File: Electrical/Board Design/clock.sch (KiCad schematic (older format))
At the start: 46 parts, among them CON1 AVR-ISP-6, CON2 USB-MICRO-B, IC1 ATTINY84A-SS, P1 CONN_6, P2 CONN_2, P3 CONN_2, Q1 FET_N, Q2 FET_P, SW1 SPST, U1 MCP1624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

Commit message: board updates
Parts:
- R1: value 100K -> 0K
- R10, R11: value 50K -> 130K
- R3: value 100K -> 10K
- R7, R8: value 36K -> 33K
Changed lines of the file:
@@
 Sheet 1 1
 Title ""
-Date "17 apr 2015"
+Date "26 apr 2015"
 Rev ""
 Comp ""
@@
 P 6550 6900
 F 0 "R7" V 6630 6900 40  0000 C CNN
-F 1 "36K" V 6557 6901 40  0000 C CNN
+F 1 "33K" V 6557 6901 40  0000 C CNN
 F 2 "~" V 6480 6900 30  0000 C CNN
 F 3 "~" H 6550 6900 30  0000 C CNN
@@
 P 6550 7750
 F 0 "R8" V 6630 7750 40  0000 C CNN
-F 1 "36K" V 6557 7751 40  0000 C CNN
+F 1 "33K" V 6557 7751 40  0000 C CNN
 F 2 "~" V 6480 7750 30  0000 C CNN
 F 3 "~" H 6550 7750 30  0000 C CNN
@@
 P 12700 3950
 F 0 "R1" V 12780 3950 40  0000 C CNN
-F 1 "100K" V 12707 3951 40  0000 C CNN
+F 1 "0K" V 12707 3951 40  0000 C CNN
 F 2 "~" V 12630 3950 30  0000 C CNN
 F 3 "~" H 12700 3950 30  0000 C CNN
@@
 P 12700 5550
 F 0 "R3" V 12780 5550 40  0000 C CNN
-F 1 "100K" V 12707 5551 40  0000 C CNN
+F 1 "10K" V 12707 5551 40  0000 C CNN
 F 2 "~" V 12630 5550 30  0000 C CNN
 F 3 "~" H 12700 5550 30  0000 C CNN
@@
 P 8400 3850
 F 0 "R11" V 8480 3850 40  0000 C CNN
-F 1 "50K" V 8407 3851 40  0000 C CNN
+F 1 "130K" V 8407 3851 40  0000 C CNN
 F 2 "~" V 8330 3850 30  0000 C CNN
 F 3 "~" H 8400 3850 30  0000 C CNN
@@
 P 10600 3850
 F 0 "R10" V 10680 3850 40  0000 C CNN
-F 1 "50K" V 10607 3851 40  0000 C CNN
+F 1 "130K" V 10607 3851 40  0000 C CNN
 F 2 "~" V 10530 3850 30  0000 C CNN
 F 3 "~" H 10600 3850 30  0000 C CNN

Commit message: release board design
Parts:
- added P4: CONN_2, symbol CONN_2
- R10, R11: value 130K -> 51K
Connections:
- net GND: now also P4.2 (PM)
- net at C7.1, CON2.1 (VBUS), U2.2 (IN): now also P4.1 (P1)
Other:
- note added: "ALTERNATE FOR USB"
- moved on the sheet: C7, CON2, U2
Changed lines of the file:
@@
 Sheet 1 1
 Title ""
-Date "26 apr 2015"
+Date "6 jun 2015"
 Rev ""
 Comp ""
@@
 P 8400 3850
 F 0 "R11" V 8480 3850 40  0000 C CNN
-F 1 "130K" V 8407 3851 40  0000 C CNN
+F 1 "51K" V 8407 3851 40  0000 C CNN
 F 2 "~" V 8330 3850 30  0000 C CNN
 F 3 "~" H 8400 3850 30  0000 C CNN
@@
 P 10600 3850
 F 0 "R10" V 10680 3850 40  0000 C CNN
-F 1 "130K" V 10607 3851 40  0000 C CNN
+F 1 "51K" V 10607 3851 40  0000 C CNN
 F 2 "~" V 10530 3850 30  0000 C CNN
 F 3 "~" H 10600 3850 30  0000 C CNN
@@
 L USB-MICRO-B CON2
 U 1 1 54A87A25
-P 1850 1450
-F 0 "CON2" H 1550 1800 50  0000 C CNN
-F 1 "USB-MICRO-B" H 1700 1100 50  0000 C CNN
-F 2 "" H 1850 1350 50  0000 C CNN
-F 3 "" H 1850 1350 50  0000 C CNN
-	1    1850 1450
+P 2550 1450
+F 0 "CON2" H 2250 1800 50  0000 C CNN
+F 1 "USB-MICRO-B" H 2400 1100 50  0000 C CNN
+F 2 "" H 2550 1350 50  0000 C CNN
+F 3 "" H 2550 1350 50  0000 C CNN
+	1    2550 1450
 	1    0    0    -1
 $EndComp
@@
 L MCP1702T-1502E/TO U2
 U 1 1 54A87F96
-P 3200 1300
-F 0 "U2" H 3000 1500 40  0000 C CNN
-F 1 "MCP1702T-1502E/TO" H 3200 1500 40  0000 L CNN
-F 2 "TO-92" H 3200 1400 30  0000 C CIN
-F 3 "~" H 3200 1300 60  0000 C CNN
-	1    3200 1300
-	1    0    0    -1
-$EndComp
-Wire Wire Line
-	2650 1250 2800 1250
-Wire Wire Line
-	3200 2050 3200 1550
-Wire Wire Line
-	3600 1250 3950 1250
-Wire Wire Line
-	3950 1250 3950 2500
-Wire Wire Line
-	3950 2500 1800 2500
+P 4050 1300
+F 0 "U2" H 3850 1500 40  0000 C CNN
+F 1 "MCP1702T-1502E/TO" H 4050 1500 40  0000 L CNN
+F 2 "TO-92" H 4050 1400 30  0000 C CIN
+F 3 "~" H 4050 1300 60  0000 C CNN
+	1    4050 1300
+	1    0    0    -1
+$EndComp
+Wire Wire Line
+	3350 1250 3650 1250
+Wire Wire Line
+	4050 2100 4050 1550
+Wire Wire Line
+	4450 1250 4700 1250
+Wire Wire Line
+	4700 1250 4700 2500
+Wire Wire Line
+	4700 2500 1800 2500
 Connection ~ 1800 3600
 Wire Wire Line
-	2650 800  2650 1400
-Wire Wire Line
-	1100 800  2650 800
-Wire Wire Line
-	1100 1250 1100 800
-Connection ~ 1100 2050
+	3350 800  3350 1400
+Wire Wire Line
+	1800 800  3350 800
+Wire Wire Line
+	1800 800  1800 1250
 $Comp
 L GND #PWR026
 U 1 1 54A88164
-P 1100 2300
-F 0 "#PWR026" H 1100 2300 30  0001 C CNN
-F 1 "GND" H 1100 2230 30  0001 C CNN
-F 2 "" H 1100 2300 60  0000 C CNN
-F 3 "" H 1100 2300 60  0000 C CNN
-	1    1100 2300
-	1    0    0    -1
-$EndComp
-Wire Wire Line
-	1100 2050 3200 2050
-Wire Wire Line
-	1100 1650 1100 2300
-Wire Wire Line
-	1350 1650 1100 1650
-Wire Wire Line
-	1350 1250 1100 1250
+P 1800 2200
+F 0 "#PWR026" H 1800 2200 30  0001 C CNN
+F 1 "GND" H 1800 2130 30  0001 C CNN
+F 2 "" H 1800 2200 60  0000 C CNN
+F 3 "" H 1800 2200 60  0000 C CNN
+	1    1800 2200
+	1    0    0    -1
+$EndComp
+Wire Wire Line
+	1800 2100 4050 2100
+Wire Wire Line
+	1800 1650 1800 2200
+Wire Wire Line
+	2050 1650 1800 1650
+Wire Wire Line
+	1800 1250 2050 1250
 $Comp
 L C C7
 U 1 1 54A89CEC
-P 2650 1600
-F 0 "C7" H 2650 1700 40  0000 L CNN
-F 1 "1uF" H 2656 1515 40  0000 L CNN
-F 2 "~" H 2688 1450 30  0000 C CNN
-F 3 "~" H 2650 1600 60  0000 C CNN
-	1    2650 1600
-	1    0    0    -1
-$EndComp
-Connection ~ 2650 1250
-Wire Wire Line
-	2650 1800 2650 2050
-Connection ~ 2650 2050
+P 3350 1600
+F 0 "C7" H 3350 1700 40  0000 L CNN
+F 1 "1uF" H 3356 1515 40  0000 L CNN
+F 2 "~" H 3388 1450 30  0000 C CNN
+F 3 "~" H 3350 1600 60  0000 C CNN
+	1    3350 1600
+	1    0    0    -1
+$EndComp
+Connection ~ 3350 1250
+Wire Wire Line
+	3350 1800 3350 2100
 Text Label 7550 4200 0    60   ~ 0
 INT 1
@@
 	1    0    0    -1
 $EndComp
+$Comp
+L CONN_2 P4
+U 1 1 55690DE7
+P 1250 1400
+F 0 "P4" V 1200 1400 40  0000 C CNN
+F 1 "CONN_2" V 1300 1400 40  0000 C CNN
+F 2 "" H 1250 1400 60  0000 C CNN
+F 3 "" H 1250 1400 60  0000 C CNN
+	1    1250 1400
+	0    -1   -1   0
+$EndComp
+Wire Wire Line
+	1350 1750 1350 1900
+Wire Wire Line
+	1350 1900 1800 1900
+Connection ~ 1800 1900
+Wire Wire Line
+	1150 1750 1150 1900
+Wire Wire Line
+	1150 1900 700  1900
+Wire Wire Line
+	700  1900 700  900
+Wire Wire Line
+	700  900  1800 900
+Connection ~ 1800 900
+Text Notes 750  1250 0    60   ~ 0
+ALTERNATE FOR USB
+Connection ~ 3350 2100
+Connection ~ 1800 2100
 $EndSCHEMATC

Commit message: saved some circuit board updates
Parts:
- added P? (x2): CONN_2, symbol CONN_2
- added Q? (x3): FET_N, ~, symbol FET_N
- added Q?: FET_P, ~, symbol FET_P
- added R? (x3): 0K, ~, symbol R
- added R? (x2): 100K, ~, symbol POT
- added R? (x2): 10K, ~, symbol R
- added R? (x2): 100K, ~, symbol R
- added SW? (x2): SPST, ~, symbol SPST
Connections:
- net ALARM LIGHT: now also P?.1 (P1)
- net AM PM LIGHT: now also P?.1 (P1)
- net GND: now also P?.2 (PM), P?.2 (PM), Q?.S, Q?.S, R?.2, R?.2, SW?.2, SW?.2
- net MODE SELECT: now also R?.2, R?.2
- net MODE SELECT POWER: now also Q?.D, Q?.S, R?.1, R?.1, R?.1, R?.1
- net VCC: now also R?.2
- net at C7.1, CON2.1 (VBUS), P4.1 (P1)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: now also R?.1
- new net: Q?.D, R?.1, R?.2
- new net: Q?.D, R?.1, R?.3
- new net: Q?.G, Q?.G, R?.2, SW?.1
- new net: Q?.S, R?.1, R?.2
- new net: Q?.D, Q?.G, R?.1, R?.3
- new net: Q?.G, R?.2, SW?.1
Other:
- note added: "connectorized clock version\nand soldered flying lead version"
- note added: "jumper to optionally\ncircumvent power blocks\nfor alarm clock version"
- moved on the sheet: D1, D2, D3, R13, R14, R15, SP1

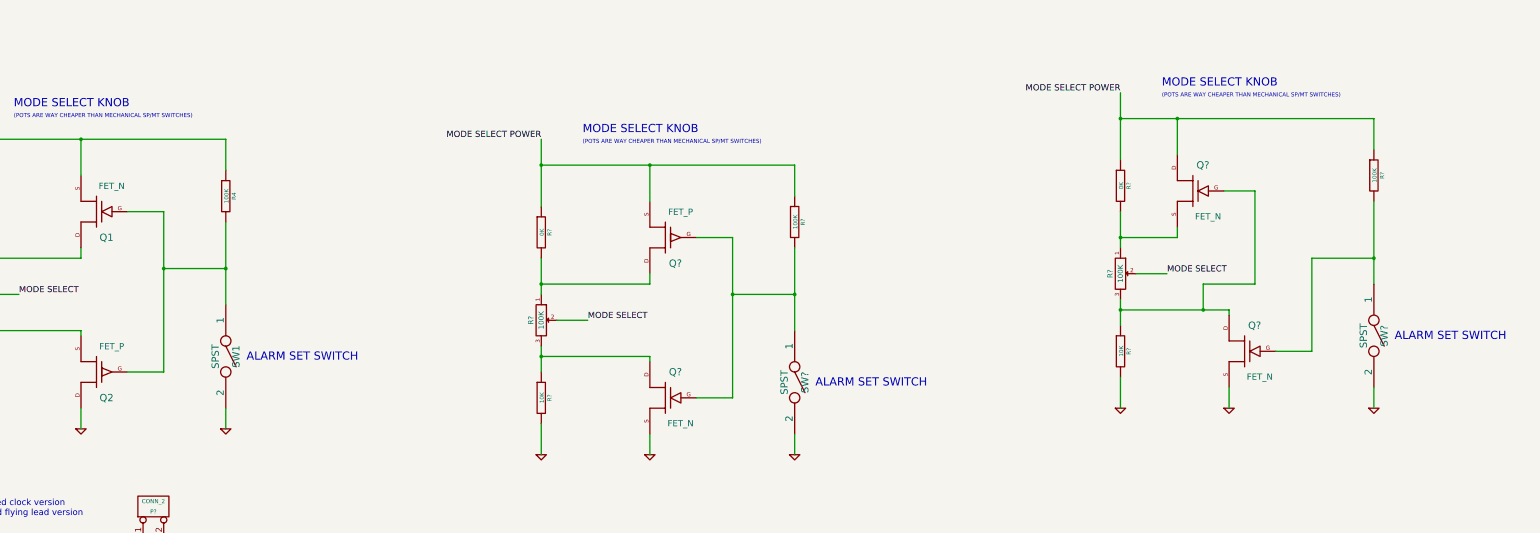
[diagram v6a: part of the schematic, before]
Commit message: fixed schematic
closes issue #17
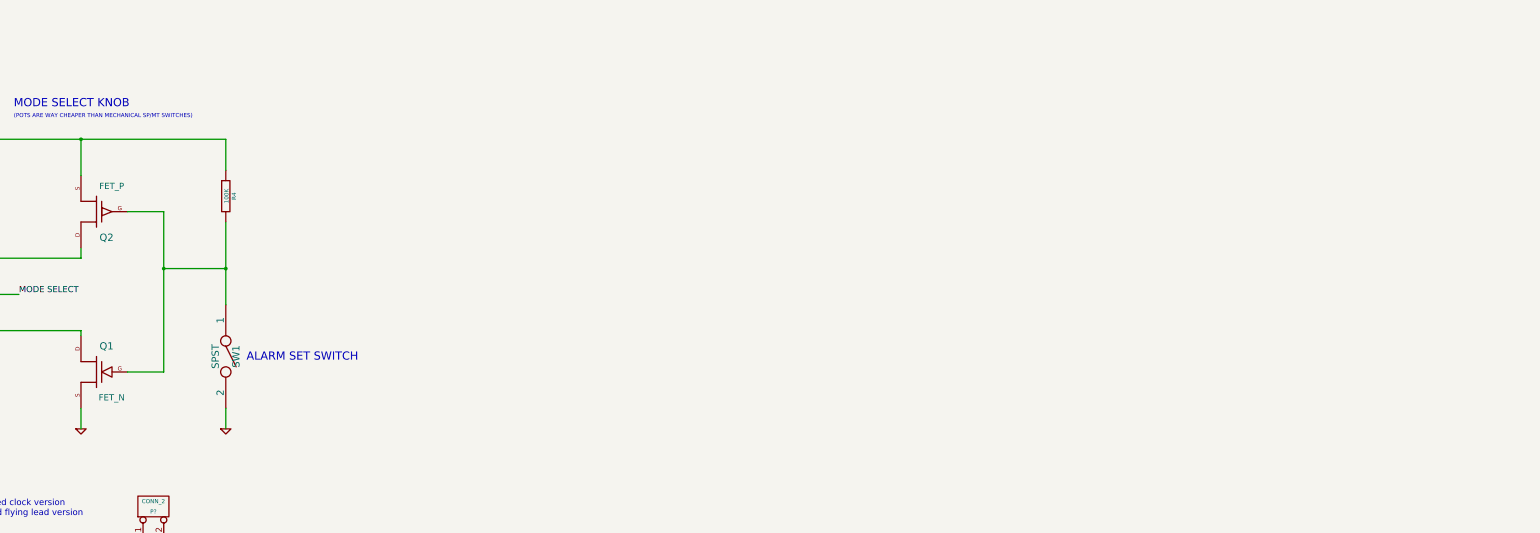
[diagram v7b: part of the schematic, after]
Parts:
- removed Q? (x3): FET_N, ~, symbol FET_N
- removed Q?: FET_P, ~, symbol FET_P
- removed R? (x2): 100K, ~, symbol POT
- removed R? (x2): 0K, ~, symbol R
- removed R? (x2): 10K, ~, symbol R
- removed R? (x2): 100K, ~, symbol R
- removed SW? (x2): SPST, ~, symbol SPST
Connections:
- net GND: now also Q1.S; no longer Q2.D
- net MODE SELECT POWER: now also Q2.S; no longer Q1.S
- net at R1.2, R2.1: now also Q2.D; no longer Q1.D
- net at R2.3, R3.1: now also Q1.D; no longer Q2.S
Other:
- moved on the sheet: Q1, Q2

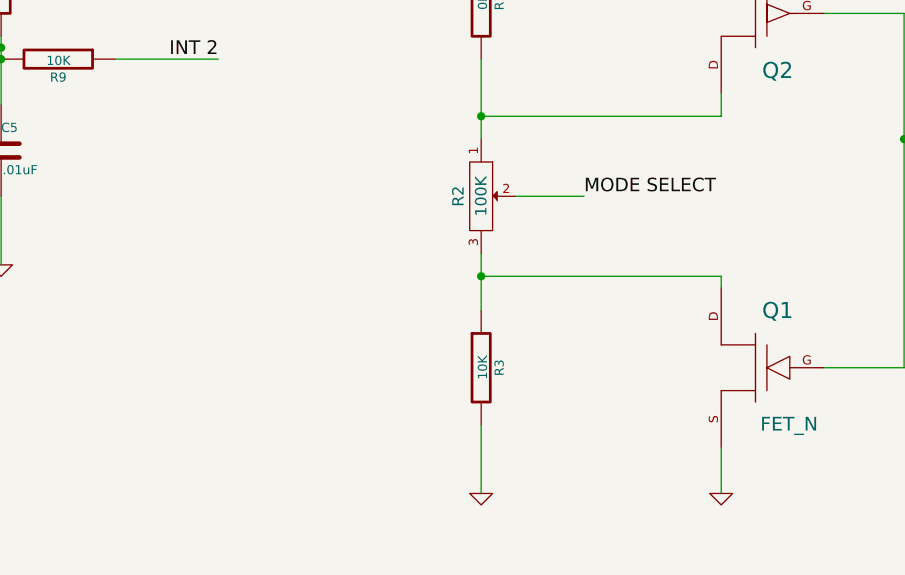
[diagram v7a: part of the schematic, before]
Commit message: add filter cap
closed issue #15
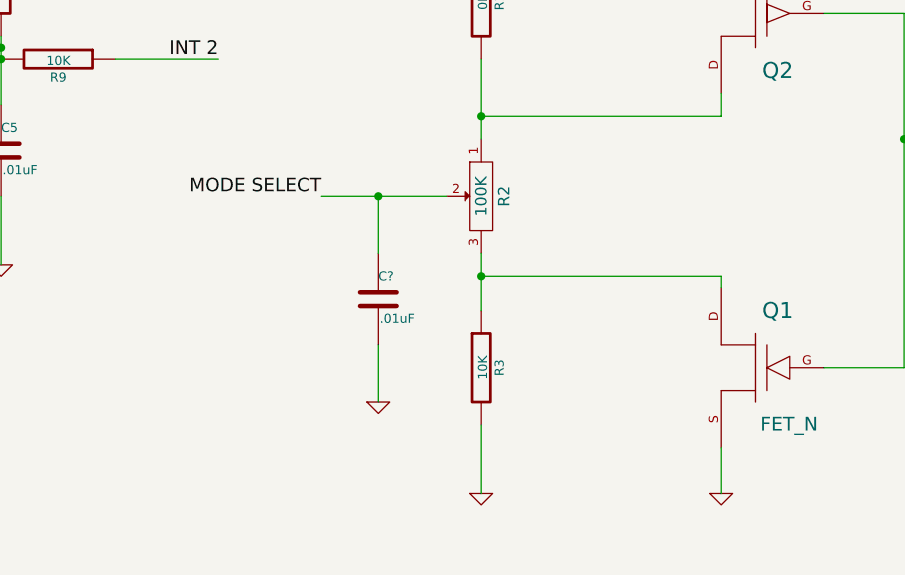
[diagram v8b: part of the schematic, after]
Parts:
- added C?: .01uF, ~, symbol C
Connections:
- net GND: now also C?.2
- net MODE SELECT: now also C?.1
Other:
- moved on the sheet: R2
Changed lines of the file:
@@
 	12700 3050 12700 3700
 Wire Wire Line
-	12850 4800 13150 4800
+	12000 4800 12550 4800
 Wire Wire Line
 	12700 5050 12700 5300
@@
 	1    0    0    -1
 $EndComp
-Text Label 13150 4800 0    59   ~ 0
+Text Label 12000 4800 2    59   ~ 0
 MODE SELECT
 $Comp
@@
 F 3 "~" H 12700 4800 60  0000 C CNN
 	1    12700 4800
-	0    1    1    0
+	0    -1   1    0
 $EndComp
 Text Notes 15350 5450 0    79   ~ 0
@@
 Text Notes 13100 3000 0    79   ~ 0
 MODE SELECT KNOB
+Wire Wire Line
+	12250 4800 12250 5050
+Connection ~ 12250 4800
+$Comp
+L C C?
+U 1 1 5632DAAC
+P 12250 5250
+F 0 "C?" H 12250 5350 40  0000 L CNN
+F 1 ".01uF" H 12256 5165 40  0000 L CNN
+F 2 "~" H 12288 5100 30  0000 C CNN
+F 3 "~" H 12250 5250 60  0000 C CNN
+	1    12250 5250
+	1    0    0    -1
+$EndComp
+Wire Wire Line
+	12250 5450 12250 5700
+$Comp
+L GND #PWR?
+U 1 1 5632DBAC
+P 12250 5700
+F 0 "#PWR?" H 12250 5700 30  0001 C CNN
+F 1 "GND" H 12250 5630 30  0001 C CNN
+F 2 "" H 12250 5700 60  0000 C CNN
+F 3 "" H 12250 5700 60  0000 C CNN
+	1    12250 5700
+	1    0    0    -1
+$EndComp
 $EndSCHEMATC
